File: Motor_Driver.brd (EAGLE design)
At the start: 87.6 x 30.1 mm, 20 parts, among them T1 2N3904, T2 2N3904, X1 M_B V+ GND M_A

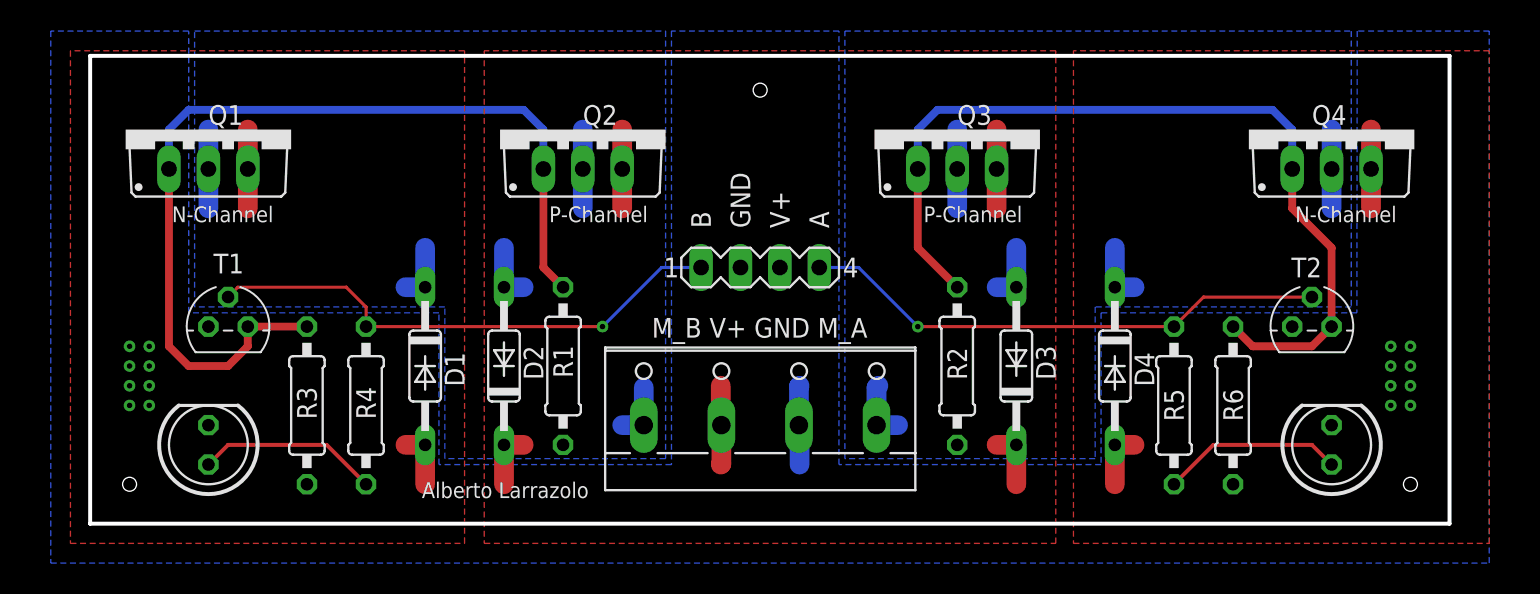
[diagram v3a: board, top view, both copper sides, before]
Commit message: Added resistors to the base of the input resistors
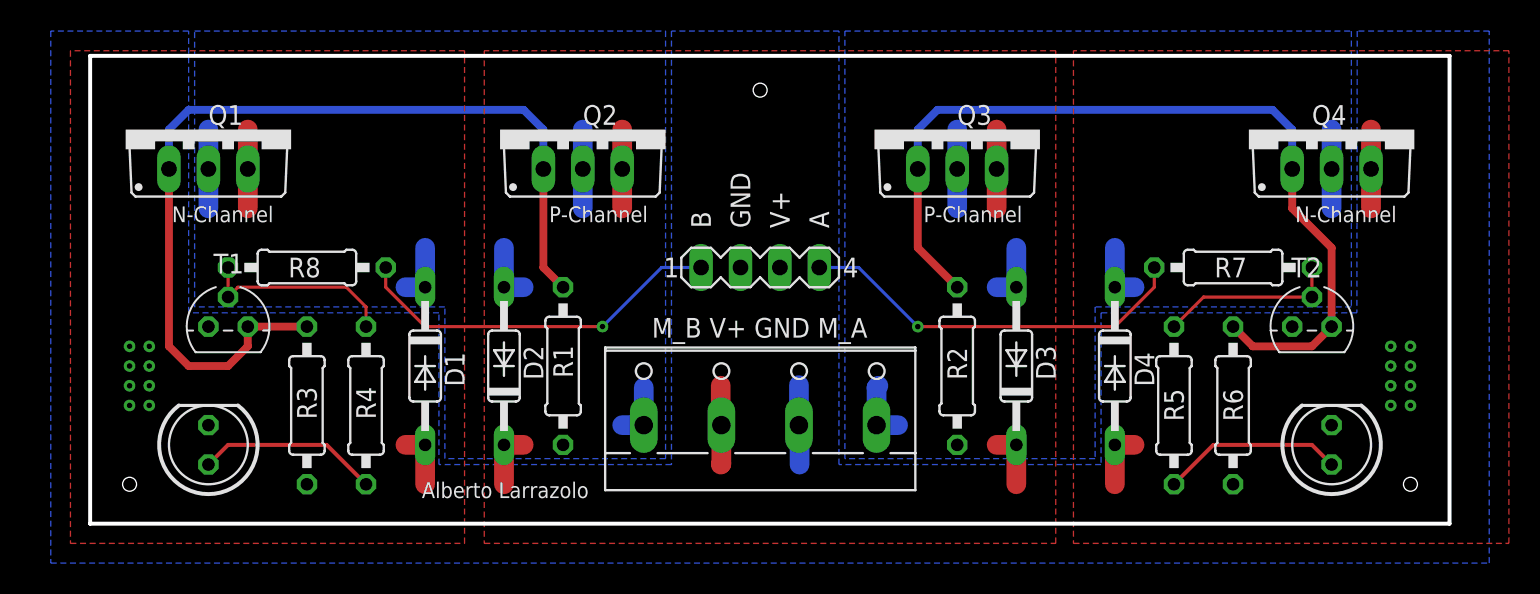
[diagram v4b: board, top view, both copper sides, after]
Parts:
- added R7, R8: 1k, resistor:0207/10
- LED1: value (none) -> LED_B
- LED2: value (none) -> LED_A
- Q1: value (none) -> N_B
- Q2: value (none) -> P_B
- Q3: value (none) -> P_A
- Q4: value (none) -> N_A
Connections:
- new net N$1: R5.2, R7.1, T2.2
- new net N$3: R4.2, R8.2, T1.2
- net INPUT_A: now also R7.2; no longer R5.2, T2.2
- net INPUT_B: now also R8.1; no longer R4.2, T1.2
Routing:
- net N$3: track 0.00 -> 12.9 mm
- net N$1: track 0.00 -> 11.6 mm
- net INPUT_B: track 34.1 -> 24.2 mm
- net INPUT_A: track 34.1 -> 25.5 mm
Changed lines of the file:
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@@
 </layers>
 <board>
-<fusionsync huburn="a.cGVyc29uYWw6dWUyYmQxNTYx" projecturn="a.cGVyc29uYWw6dWUyYmQxNTYxIzIwMTcwNTAzNzQ1OTM2NTY" f3durn="urn:adsk.wipprod:dm.lineage:4LoYFpwRT0WNoFuGUnykHQ" pcbguid="78764fb1-ee6b-49c0-b5bc-c6e3655d7beb" lastpulledtime="2019-02-07T21:09:33Z" lastsyncedchangeguid="b2fdb641-c53b-a119-a0bc-a5a252d5b16f"/>
+<fusionsync huburn="a.cGVyc29uYWw6dWUyYmQxNTYx" projecturn="a.cGVyc29uYWw6dWUyYmQxNTYxIzIwMTcwNTAzNzQ1OTM2NTY" f3durn="urn:adsk.wipprod:dm.lineage:4LoYFpwRT0WNoFuGUnykHQ" pcbguid="78764fb1-ee6b-49c0-b5bc-c6e3655d7beb" lastpulledtime="2019-02-07T21:09:33Z" lastsyncedchangeguid="d810249e-5192-ccfa-566a-b22169730ef7"/>
 <plain>
 <text x="32.131" y="2.667" size="1.016" layer="21" font="vector" rot="R180">Alberto Larrazolo</text>
@@
 </autorouter>
 <elements>
-<element name="LED2" library="led" library_urn="urn:adsk.eagle:library:259" package="LED5MM" package3d_urn="urn:adsk.eagle:package:15799/2" value="" x="80.01" y="5.08" smashed="yes" rot="R90">
+<element name="LED2" library="led" library_urn="urn:adsk.eagle:library:259" package="LED5MM" package3d_urn="urn:adsk.eagle:package:15799/2" value="LED_A" x="80.01" y="5.08" smashed="yes" rot="R90">
 <attribute name="VALUE" x="81.8134" y="8.2804" size="1.27" layer="27" ratio="10" rot="R90"/>
 </element>
-<element name="Q4" library="transistor-power" library_urn="urn:adsk.eagle:library:400" package="TO220BV" package3d_urn="urn:adsk.eagle:package:29484/3" value="" x="80.01" y="25.4" smashed="yes">
+<element name="Q4" library="transistor-power" library_urn="urn:adsk.eagle:library:400" package="TO220BV" package3d_urn="urn:adsk.eagle:package:29484/3" value="N_A" x="80.01" y="25.4" smashed="yes">
 <attribute name="NAME" x="78.74" y="25.7048" size="1.27" layer="25" font="vector" ratio="10"/>
 <attribute name="VALUE" x="74.93" y="17.78" size="1.27" layer="27" ratio="10"/>
 </element>
-<element name="Q1" library="transistor-power" library_urn="urn:adsk.eagle:library:400" package="TO220BV" package3d_urn="urn:adsk.eagle:package:29484/3" value="" x="7.62" y="25.4" smashed="yes">
+<element name="Q1" library="transistor-power" library_urn="urn:adsk.eagle:library:400" package="TO220BV" package3d_urn="urn:adsk.eagle:package:29484/3" value="N_B" x="7.62" y="25.4" smashed="yes">
 <attribute name="NAME" x="7.62" y="25.7048" size="1.27" layer="25" font="vector" ratio="10"/>
 <attribute name="VALUE" x="2.54" y="17.78" size="1.27" layer="27" ratio="10"/>
 </element>
-<element name="Q3" library="transistor-power" library_urn="urn:adsk.eagle:library:400" package="TO220BV" package3d_urn="urn:adsk.eagle:package:29484/3" value="" x="55.88" y="25.4" smashed="yes">
+<element name="Q3" library="transistor-power" library_urn="urn:adsk.eagle:library:400" package="TO220BV" package3d_urn="urn:adsk.eagle:package:29484/3" value="P_A" x="55.88" y="25.4" smashed="yes">
 <attribute name="NAME" x="55.88" y="25.7048" size="1.27" layer="25" font="vector" ratio="10"/>
 <attribute name="VALUE" x="50.8" y="17.78" size="1.27" layer="27" ratio="10"/>
 </element>
-<element name="Q2" library="transistor-power" library_urn="urn:adsk.eagle:library:400" package="TO220BV" package3d_urn="urn:adsk.eagle:package:29484/3" value="" x="31.75" y="25.4" smashed="yes">
+<element name="Q2" library="transistor-power" library_urn="urn:adsk.eagle:library:400" package="TO220BV" package3d_urn="urn:adsk.eagle:package:29484/3" value="P_B" x="31.75" y="25.4" smashed="yes">
 <attribute name="NAME" x="31.75" y="25.7048" size="1.27" layer="25" font="vector" ratio="10"/>
 <attribute name="VALUE" x="26.67" y="17.78" size="1.27" layer="27" ratio="10"/>
@@
 <attribute name="NAME" x="14.605" y="6.731" size="1.27" layer="25" font="vector" ratio="10" rot="R90"/>
 </element>
-<element name="LED1" library="led" library_urn="urn:adsk.eagle:library:259" package="LED5MM" package3d_urn="urn:adsk.eagle:package:15799/2" value="" x="7.62" y="5.08" smashed="yes" rot="R90">
+<element name="LED1" library="led" library_urn="urn:adsk.eagle:library:259" package="LED5MM" package3d_urn="urn:adsk.eagle:package:15799/2" value="LED_B" x="7.62" y="5.08" smashed="yes" rot="R90">
 <attribute name="VALUE" x="9.4234" y="8.2804" size="1.27" layer="27" ratio="10" rot="R90"/>
 </element>
@@
 <attribute name="OC_NEWARK" value="unknown" x="43.18" y="7.62" size="1.778" layer="27" display="off"/>
 <attribute name="VALUE" x="43.1476" y="13.2588" size="1.27" layer="25" ratio="10" align="top-center"/>
+</element>
+<element name="R7" library="resistor" library_urn="urn:adsk.eagle:library:348" package="0207/10" package3d_urn="urn:adsk.eagle:package:23491/2" value="1k" x="73.66" y="16.51" smashed="yes" rot="R180">
+<attribute name="NAME" x="74.549" y="17.145" size="1.27" layer="25" ratio="10" rot="R180"/>
+<attribute name="VALUE" x="75.9206" y="17.145" size="1.27" layer="27" ratio="10" rot="R180"/>
+</element>
+<element name="R8" library="resistor" library_urn="urn:adsk.eagle:library:348" package="0207/10" package3d_urn="urn:adsk.eagle:package:23491/2" value="1k" x="13.97" y="16.51" smashed="yes" rot="R180">
+<attribute name="NAME" x="14.859" y="17.145" size="1.27" layer="25" ratio="10" rot="R180"/>
+<attribute name="VALUE" x="16.2306" y="17.145" size="1.27" layer="27" ratio="10" rot="R180"/>
 </element>
 </elements>
@@
 <vertex x="63.373" y="30.48"/>
 <vertex x="63.373" y="-1.27"/>
-<vertex x="90.17" y="-1.27"/>
-<vertex x="90.17" y="30.48"/>
+<vertex x="91.44" y="-1.27"/>
+<vertex x="91.44" y="30.48"/>
 </polygon>
 <contactref element="T1" pad="3"/>
@@
 <wire x1="10.16" y1="22.86" x2="10.16" y2="20.32" width="1.27" layer="1"/>
 <wire x1="10.16" y1="22.86" x2="10.16" y2="25.4" width="1.27" layer="1"/>
-<wire x1="45.68" y1="6.35" x2="45.68" y2="8.85" width="1.27" layer="16"/>
-<wire x1="45.68" y1="8.85" x2="45.72" y2="8.89" width="1.27" layer="16"/>
-<wire x1="45.68" y1="6.35" x2="45.72" y2="6.31" width="1.27" layer="16"/>
-<wire x1="45.72" y1="6.31" x2="45.72" y2="3.81" width="1.27" layer="16"/>
 <wire x1="21.59" y1="5.08" x2="21.59" y2="2.54" width="1.27" layer="1"/>
 <wire x1="21.59" y1="5.08" x2="20.32" y2="5.08" width="1.27" layer="1"/>
 <wire x1="66.04" y1="5.08" x2="66.04" y2="2.54" width="1.27" layer="1"/>
 <wire x1="66.04" y1="5.08" x2="67.31" y2="5.08" width="1.27" layer="1"/>
+<wire x1="45.68" y1="6.35" x2="45.68" y2="8.93" width="1.27" layer="16"/>
+<wire x1="45.68" y1="6.35" x2="45.72" y2="6.31" width="1.27" layer="16"/>
+<wire x1="45.72" y1="6.31" x2="45.72" y2="3.81" width="1.27" layer="16"/>
 </signal>
 <signal name="INPUT_A">
-<contactref element="R5" pad="2"/>
-<contactref element="T2" pad="2"/>
 <contactref element="SV1" pad="4"/>
 <wire x1="46.99" y1="16.51" x2="49.53" y2="16.51" width="0.2032" layer="16"/>
 <wire x1="49.53" y1="16.51" x2="53.34" y2="12.7" width="0.2032" layer="16"/>
 <via x="53.34" y="12.7" extent="1-16" drill="0.35"/>
-<wire x1="53.34" y1="12.7" x2="69.85" y2="12.7" width="0.2032" layer="1"/>
-<wire x1="69.85" y1="12.7" x2="71.755" y2="14.605" width="0.2032" layer="1"/>
-<wire x1="71.755" y1="14.605" x2="78.74" y2="14.605" width="0.2032" layer="1"/>
+<contactref element="R7" pad="2"/>
+<wire x1="53.34" y1="12.7" x2="66.04" y2="12.7" width="0.2032" layer="1"/>
+<wire x1="66.04" y1="12.7" x2="68.58" y2="15.24" width="0.2032" layer="1"/>
+<wire x1="68.58" y1="15.24" x2="68.58" y2="16.51" width="0.2032" layer="1"/>
 </signal>
 <signal name="INPUT_B">
-<contactref element="R4" pad="2"/>
-<contactref element="T1" pad="2"/>
 <contactref element="SV1" pad="1"/>
 <wire x1="39.37" y1="16.51" x2="36.83" y2="16.51" width="0.2032" layer="16"/>
 <wire x1="36.83" y1="16.51" x2="33.02" y2="12.7" width="0.2032" layer="16"/>
 <via x="33.02" y="12.7" extent="1-16" drill="0.35"/>
-<wire x1="33.02" y1="12.7" x2="17.78" y2="12.7" width="0.2032" layer="1"/>
+<contactref element="R8" pad="1"/>
+<wire x1="33.02" y1="12.7" x2="21.59" y2="12.7" width="0.2032" layer="1"/>
+<wire x1="21.59" y1="12.7" x2="19.05" y2="15.24" width="0.2032" layer="1"/>
+<wire x1="19.05" y1="15.24" x2="19.05" y2="16.51" width="0.2032" layer="1"/>
+</signal>
+<signal name="N$1">
+<contactref element="R5" pad="2"/>
+<contactref element="T2" pad="2"/>
+<contactref element="R7" pad="1"/>
+<wire x1="69.85" y1="12.7" x2="71.755" y2="14.605" width="0.2032" layer="1"/>
+<wire x1="71.755" y1="14.605" x2="78.74" y2="14.605" width="0.2032" layer="1"/>
+<wire x1="78.74" y1="16.51" x2="78.74" y2="14.605" width="0.2032" layer="1"/>
+</signal>
+<signal name="N$3">
+<contactref element="R4" pad="2"/>
+<contactref element="T1" pad="2"/>
+<contactref element="R8" pad="2"/>
 <wire x1="8.89" y1="14.605" x2="9.525" y2="15.24" width="0.2032" layer="1"/>
 <wire x1="16.51" y1="15.24" x2="9.525" y2="15.24" width="0.2032" layer="1"/>
 <wire x1="17.78" y1="12.7" x2="17.78" y2="13.97" width="0.2032" layer="1"/>
 <wire x1="17.78" y1="13.97" x2="16.51" y2="15.24" width="0.2032" layer="1"/>
+<wire x1="8.89" y1="16.51" x2="8.89" y2="14.605" width="0.2032" layer="1"/>
 </signal>
 </signals>
@@
 <mfgpreviewcolor name="substratecolor" color="0xFF786E46"/>
 </mfgpreviewcolors>
+<errors>
+</errors>
 </board>
 </drawing>
